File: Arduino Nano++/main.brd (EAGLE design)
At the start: 68.6 x 53.3 mm, 68 parts, among them IC1 LM358N, Q1 IRF9530, Q2 IRF9530

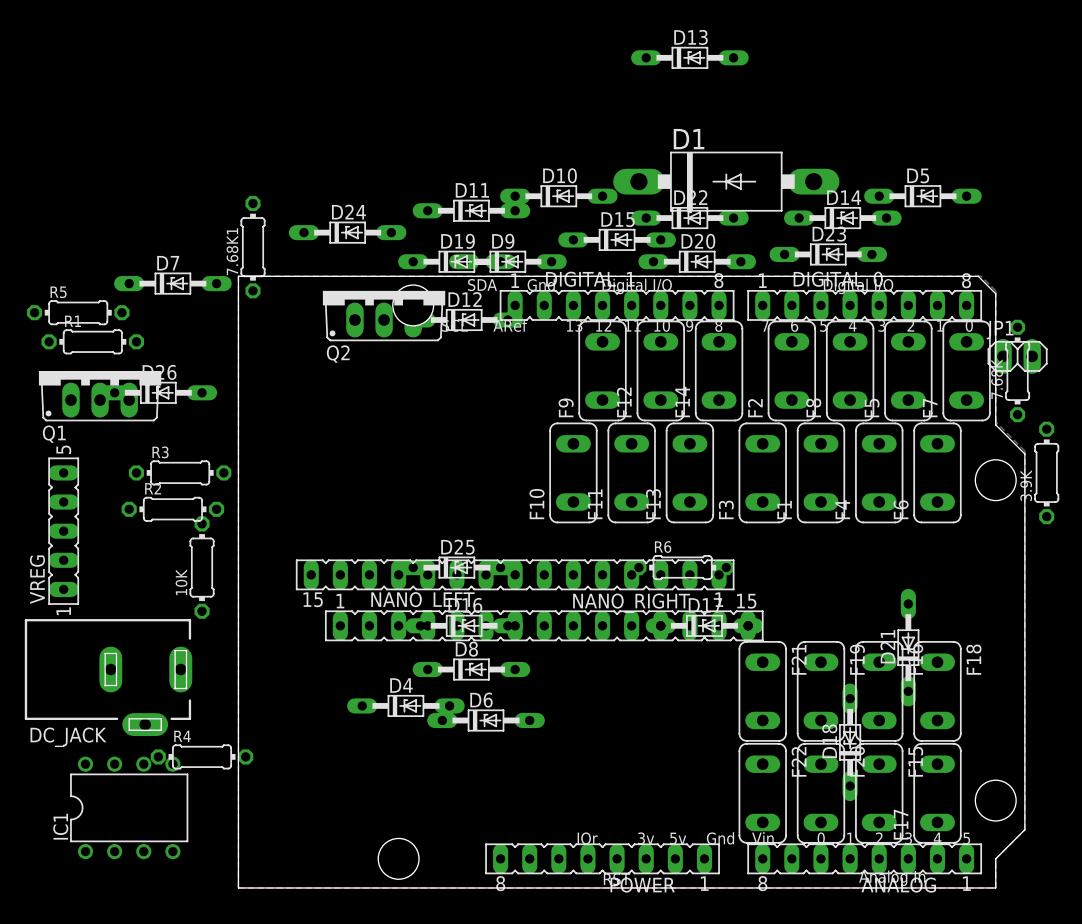
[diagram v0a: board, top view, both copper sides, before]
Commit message: Nano++ schematic; guitar hero redo to not use 1/64th bit
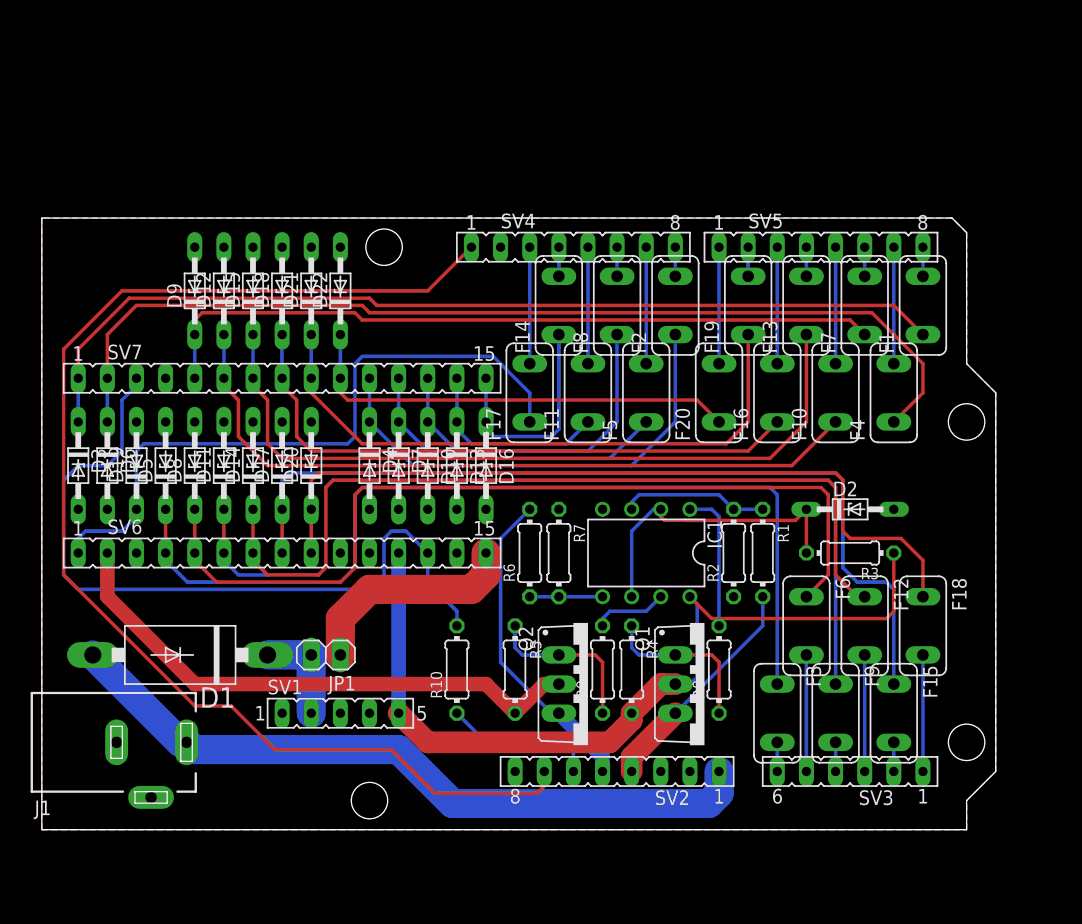
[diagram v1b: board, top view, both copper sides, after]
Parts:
- removed 10K, 3.9K, 7.68K, 7.68K1: (no value), rcl:0204/7
- removed ANALOG, DIGITAL_0, DIGITAL_1, POWER: (no value), con-lsta:FE08
- removed D23, D24, D25, D26: BZX90, diode:DO34Z7
- removed DC_JACK: (no value), con-jack:DCJ0303
- removed F21, F22: FUSETE5, fuse:TE5
- removed NANO_LEFT, NANO_RIGHT: (no value), con-lsta:FE15
- removed VREG: (no value), con-lsta:FE05-1
- added D2, D3: BZX90, diode:DO34Z7
- added J1: (no value), con-jack:DCJ0303
- added R10: 1k, rcl:0204/7
- added R7: (no value), rcl:0204/7
- added R8, R9: 300, rcl:0204/7
- added SV1: (no value), con-lsta:FE05-1
- added SV2, SV4, SV5: (no value), con-lsta:FE08
- added SV3: (no value), con-lsta:FE06
- added SV6, SV7: (no value), con-lsta:FE15
- R2: value 10k -> (none)
- R3: value 300 -> (none)
- R5: value 300 -> 10k
- R6: value 1k -> (none)
- moved D5 70.1 mm to (11.4, 52.1), turned to 90 degrees
- moved JP1 65.7 mm to (25.4, 35.6), turned to 180 degrees
- moved D18 63.3 mm to (21.6, 67.3)
- moved D1 63.0 mm to (12.7, 35.6), turned to 180 degrees
- moved R1 61.3 mm to (63.5, 44.5), turned to 270 degrees
- moved D21 60.7 mm to (24.1, 67.3)
- moved Q1 59.4 mm to (58.4, 33.0), turned to 270 degrees
- moved R3 58.8 mm to (71.1, 44.5), turned to 180 degrees
- moved D14 55.8 mm to (19.1, 52.1), turned to 90 degrees
- moved IC1 50.3 mm to (53.3, 44.5), turned to 180 degrees
- moved F17 49.8 mm to (43.2, 58.4)
- moved R5 49.2 mm to (41.9, 34.3), turned to 270 degrees
- moved R2 49.0 mm to (61.0, 44.5), turned to 90 degrees
- moved D13 41.0 mm to (36.8, 52.1), turned to 270 degrees
- moved D6 39.8 mm to (6.35, 52.1), turned to 270 degrees
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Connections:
- removed net A6: D20.C, F17.1, NANO_LEFT.10
- removed net A6': ANALOG.2, F17.2
- removed net A7: D21.C, F18.1, NANO_LEFT.11
- removed net A7': ANALOG.1, F18.2
- removed net N$1: POWER.8
- net 3V3: now also R5.2, SV6.2; no longer NANO_LEFT.2, R4.2
- net 3V3': now also R6.2, SV2.5; no longer 3.9K.2, POWER.5
- net 3V3EN: now also R9.2; no longer R5.2
- net 5V: now also R3.1, R4.2, SV1.5, SV6.12; no longer NANO_LEFT.12, R1.1, R2.2, VREG.5
- net 5V': now also R1.2, SV2.4; no longer 10K.2, POWER.4
- net 5VEN: now also R8.2; no longer R3.2
- net A0: now also D5.C, F3.1, SV6.4; no longer D25.C, F22.1, NANO_LEFT.4
- net A0': now also F3.2, SV3.6; no longer ANALOG.8, F22.2
- net A1: now also D8.C, F6.1, SV6.5; no longer D24.C, F21.1, NANO_LEFT.5
- net A1': now also F6.2, SV3.5; no longer ANALOG.7, F21.2
- net A2: now also D11.C, F9.1, SV6.6; no longer D23.C, F20.1, NANO_LEFT.6
- net A2': now also F9.2, SV3.4; no longer ANALOG.6, F20.2
- net A3: now also D14.C, F12.1, SV6.7; no longer D22.C, F19.1, NANO_LEFT.7
- net A3': now also F12.2, SV3.3; no longer ANALOG.5, F19.2
- net A4: now also D17.C, SV6.8; no longer D18.C, NANO_LEFT.8
- net A4': now also SV3.2; no longer ANALOG.4
- net A5: now also D20.C, F18.1, SV6.9; no longer D19.C, F16.1, NANO_LEFT.9
- net A5': now also F18.2, SV3.1; no longer ANALOG.3, F16.2
- net AREF: now also SV6.3; no longer NANO_LEFT.3
- net AREF': now also SV2.7, SV4.1; no longer DIGITAL_1.1, POWER.7
- net D0: now also D3.C, F1.1, SV7.1; no longer D11.C, F7.1, NANO_RIGHT.1
- net D0': now also F1.2, SV5.8; no longer DIGITAL_0.8, F7.2
- net D1: now also D6.C, F4.1, SV7.2; no longer D10.C, F6.1, NANO_RIGHT.2
- net D1': now also F4.2, SV5.7; no longer DIGITAL_0.7, F6.2
- net D10: now also D10.C, F8.1, SV7.13; no longer D15.C, F12.1, NANO_RIGHT.13
- net D10': now also F8.2, SV4.6; no longer DIGITAL_1.6, F12.2
- net D11: now also D13.C, SV7.14; no longer D14.C, NANO_RIGHT.14
- net D11': now also SV4.5; no longer DIGITAL_1.5
- net D12: now also D16.C, F14.1, SV7.15; no longer D12.C, F9.1, NANO_RIGHT.15
- net D12': now also F14.2, SV4.4; no longer DIGITAL_1.4, F9.2
- net D13: now also D19.C, F17.1, SV6.1; no longer D13.C, F10.1, NANO_LEFT.1
- net D13': now also F17.2, SV4.3; no longer DIGITAL_1.3, F10.2
- net D2: now also F7.1, SV7.5; no longer F5.1, NANO_RIGHT.5
- net D2': now also F7.2, SV5.6; no longer DIGITAL_0.6, F5.2
- net D3: now also D12.C, F10.1, SV7.6; no longer D8.C, F4.1, NANO_RIGHT.6
- net D3': now also F10.2, SV5.5; no longer DIGITAL_0.5, F4.2
- net D4: now also D15.C, F13.1, SV7.7; no longer D5.C, F8.1, NANO_RIGHT.7
- net D4': now also F13.2, SV5.4; no longer DIGITAL_0.4, F8.2
- net D5: now also D18.C, F16.1, SV7.8; no longer D4.C, F1.1, NANO_RIGHT.8
- net D5': now also F16.2, SV5.3; no longer DIGITAL_0.3, F1.2
- net D6: now also D21.C, F19.1, SV7.9; no longer D6.C, F2.1, NANO_RIGHT.9
- net D6': now also F19.2, SV5.2; no longer DIGITAL_0.2, F2.2
- net D7: now also D22.C, F20.1, SV7.10; no longer D7.C, F3.1, NANO_RIGHT.10
- net D7': now also F20.2, SV5.1; no longer DIGITAL_0.1, F3.2
- net D8: now also D4.C, F2.1, SV7.11; no longer D17.C, F14.1, NANO_RIGHT.11
- net D8': now also F2.2, SV4.8; no longer DIGITAL_1.8, F14.2
- net D9: now also D7.C, F5.1, SV7.12; no longer D16.C, F13.1, NANO_RIGHT.12
- net D9': now also F5.2, SV4.7; no longer DIGITAL_1.7, F13.2
- net GND: now also D2.A, D3.A, J1.3, R2.1, R7.1, SV1.3, SV1.4, SV2.2, SV2.3, SV4.2, SV6.14, SV7.4; no longer 7.68K.1, 7.68K1.1, D23.A, D24.A, D25.A, D26.A, DC_JACK.3, DIGITAL_1.2, NANO_LEFT.14, NANO_RIGHT.4, POWER.2, POWER.3, VREG.3, VREG.4
- net N$2: now also SV1.2; no longer VREG.2
- net N$3: now also R9.1; no longer R4.1
- net N$4: now also R4.1, R8.1; no longer R2.1, R3.1
- net N$6: now also R1.1, R2.2; no longer 10K.1, 7.68K.2
- net N$7: now also R6.1, R7.2; no longer 3.9K.1, 7.68K1.2
- net RST: now also R10.2, SV6.13, SV7.3; no longer NANO_LEFT.13, NANO_RIGHT.3, R6.2
- net RST': now also R10.1, SV2.6; no longer POWER.6, R6.1
- net VIN: now also SV6.15
- net VIN': now also J1.1, SV2.1; no longer DC_JACK.1, POWER.1
- net VREF2.4: now also D2.C, R3.2; no longer D26.C, R1.2
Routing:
- net AREF': track 0.00 -> 110.3 mm
- net D1: track 0.00 -> 88.0 mm
- net A2: track 0.00 -> 83.2 mm
- net D0: track 0.00 -> 83.2 mm
- net A0: track 0.00 -> 82.5 mm
- net A1: track 0.00 -> 77.6 mm
- net A4: track 0.00 -> 76.9 mm
- net 5V: track 0.00 -> 75.0 mm
- net A3: track 0.00 -> 74.5 mm
- net A5: track 0.00 -> 68.9 mm
- net D4: track 0.00 -> 66.5 mm
- net RST: track 0.00 -> 65.7 mm
- net D2: track 0.00 -> 64.6 mm
- net D3: track 0.00 -> 64.1 mm
- net VIN': track 0.00 -> 62.2 mm
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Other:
- board size 68.6 x 53.3 mm -> 83.2 x 53.3 mm
- board text added: "!RESET!"
- board text added: "3.3V"
- board text added: "5V"
- board text added: ">NAME"
- board text added: ">VALUE"
- board text added: "A0"
- board text added: "A1"
- board text added: "A2"
- board text added: "A3"
- board text added: "A4"
- board text added: "A5"
- board text added: "AREF"
- board text added: "D0/RXI"
- board text added: "D1/TXO"
- board text added: "D10"
- board text added: "D11"
- board text added: "D12"
- board text added: "D13"
- board text added: "D2"
- board text added: "D3"
- board text added: "D4"
- board text added: "D5"
- board text added: "D6"
- board text added: "D7"
- board text added: "D8"
- board text added: "D9"
- board text added: "GND"
- board text added: "IOREF"
- board text added: "MISO"
- board text added: "MOSI"
- board text added: "SCK"
- board text added: "VIN"
- board text removed: "0"
- board text removed: "1"
- board text removed: "10"
- board text removed: "11"
- board text removed: "12"
- board text removed: "13"
- board text removed: "2"
- board text removed: "3"
- board text removed: "3v"
- board text removed: "4"
- board text removed: "5"
- board text removed: "5v"
- board text removed: "6"
- board text removed: "7"
- board text removed: "8"
- board text removed: "9"
- board text removed: "ARef"
- board text removed: "Analog In"
- board text removed: "Digital I/O"
- board text removed: "Gnd"
- board text removed: "IOr"
- board text removed: "Vin"
